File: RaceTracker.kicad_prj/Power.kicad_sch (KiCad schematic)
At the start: 41 parts, among them J1 USB-C Sink, J7 LiPo, Q2 SIA817, Q3 2N7002, U3 AP2112K-3.3 -> +3V3D, U5 BQ24195L, U6 AP2112K-3.3 -> +3V3

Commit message: Footprints für Power+MCU_Radio: aus MKR1010-Eagle-Referenz importiert
Nutzt kicad-cli pcb import, um die reale MKR-WiFi-1010-Platine
(user-bereitgestellt, MKRWiFi1010V2.0.brd) nach KiCad zu konvertieren
und daraus bewährte, aus einem tatsächlich gefertigten Board stammende
Footprint-Geometrien zu extrahieren statt sie zu schätzen:

- 15 spezielle Footprints neu in RaceTracker.pretty/ (SOT-143B für D1,
  SOD-323FL für D2/D3, SOT-523 für Q1/Q3, SON-8 für Q2, SOT-363 für Q5,
  JST-PH für J7, PTS820-Taster, 0603-LED, RGB-5050-LED, SRP4020-Spule,
  32.768kHz-Quarz ABS07)
- 3 bestehende Custom-Footprints (QFN24, QFN48/SAMD21, NINA-W1X) durch
  die vollständigeren Eagle-Varianten ersetzt (identische Pad-Namen
  verifiziert, jetzt mit Silkscreen-Outline und Lötstoppmasken-Angaben)
- Alle Standard-Passiva (R/C 0402/0603/0805, Fuse, Ferritperle) auf
  KiCads Standardbibliothek gemappt
- J12 (SWD-Header) auf Standard-2,54mm-5-Pin-Stiftleiste gemappt

87 von 90 Bauteilen auf Power+MCU_Radio haben jetzt ein Footprint
(Rest: GPS- und Sensors_Storage-Blatt folgen). ERC weiterhin 0/0,
inklusive der Footprint-Bibliotheksprüfung (jeder Footprint-Name
gegen die echte Bibliothek verifiziert).

Co-Authored-By: Claude Sonnet 5 <noreply@anthropic.com>
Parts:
- C1: footprint (none) -> Capacitor_SMD:C_0805_2012Metric
- C12, C13, C19, C20: footprint (none) -> Capacitor_SMD:C_0603_1608Metric
- C14, C15, C16, C22, C32, C33, C34, C8, C9: footprint (none) -> Capacitor_SMD:C_0402_1005Metric
- D1: footprint (none) -> RaceTracker:SOT143B_4N
- D2, D3: footprint (none) -> RaceTracker:SODFL3517X110N
- DL2, DL3: footprint (none) -> RaceTracker:LED_0603_AK
- F1, F2: footprint (none) -> Fuse:Fuse_0603_1608Metric
- J7: footprint (none) -> RaceTracker:JST_S2B_PH_SM4_TB
- L2: footprint (none) -> RaceTracker:SRP4020
- Q2: footprint (none) -> RaceTracker:SON65P205X205X75-8N-MWSD
- Q3: footprint (none) -> RaceTracker:SOTFL50P160X78-3
- R1, R19, R23, R24, R25, R26, R27, R28, R29, R30, R37, R38: footprint (none) -> Resistor_SMD:R_0402_1005Metric
- U3, U6: footprint (none) -> RaceTracker:SOT25
- U5: footprint (none) -> RaceTracker:QFN24_BQ24195L
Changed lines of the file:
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@@
 			)
 		)
-		(property "Footprint" ""
+		(property "Footprint" "Resistor_SMD:R_0402_1005Metric"
 			(at 134.62 43.18 0)
 			(hide yes)
@@
 			)
 		)
-		(property "Footprint" ""
+		(property "Footprint" "RaceTracker:SODFL3517X110N"
 			(at 248.92 43.18 0)
 			(hide yes)
@@
 			)
 		)
-		(property "Footprint" ""
+		(property "Footprint" "Capacitor_SMD:C_0402_1005Metric"
 			(at 170.18 97.79 0)
 			(hide yes)
@@
 			)
 		)
-		(property "Footprint" ""
+		(property "Footprint" "RaceTracker:SOT25"
 			(at 297.18 152.4 0)
 			(hide yes)
@@
 			)
 		)
-		(property "Footprint" ""
+		(property "Footprint" "Capacitor_SMD:C_0402_1005Metric"
 			(at 231.14 97.79 0)
 			(hide yes)
@@
 			)
 		)
-		(property "Footprint" ""
+		(property "Footprint" "RaceTracker:SRP4020"
 			(at 68.58 97.79 0)
 			(hide yes)
@@
 			)
 		)
-		(property "Footprint" ""
+		(property "Footprint" "RaceTracker:SODFL3517X110N"
 			(at 372.11 43.18 0)
 			(hide yes)
@@
 			)
 		)
-		(property "Footprint" ""
+		(property "Footprint" "RaceTracker:SOT143B_4N"
 			(at 67.31 43.18 0)
 			(hide yes)
@@
 			)
 		)
-		(property "Footprint" ""
+		(property "Footprint" "RaceTracker:SOT25"
 			(at 251.46 152.4 0)
 			(hide yes)
@@
 			)
 		)
-		(property "Footprint" ""
+		(property "Footprint" "Capacitor_SMD:C_0402_1005Metric"
 			(at 330.2 152.4 0)
 			(hide yes)
@@
 			)
 		)
-		(property "Footprint" ""
+		(property "Footprint" "RaceTracker:SON65P205X205X75-8N-MWSD"
 			(at 275.59 43.18 0)
 			(hide yes)
@@
 			)
 		)
-		(property "Footprint" ""
+		(property "Footprint" "Capacitor_SMD:C_0603_1608Metric"
 			(at 109.22 97.79 0)
 			(hide yes)
@@
 			)
 		)
-		(property "Footprint" ""
+		(property "Footprint" "Resistor_SMD:R_0402_1005Metric"
 			(at 93.98 43.18 0)
 			(hide yes)
@@
 			)
 		)
-		(property "Footprint" ""
+		(property "Footprint" "Resistor_SMD:R_0402_1005Metric"
 			(at 154.94 43.18 0)
 			(hide yes)
@@
 			)
 		)
-		(property "Footprint" ""
+		(property "Footprint" "Resistor_SMD:R_0402_1005Metric"
 			(at 83.82 152.4 0)
 			(hide yes)
@@
 			)
 		)
-		(property "Footprint" ""
+		(property "Footprint" "Capacitor_SMD:C_0603_1608Metric"
 			(at 129.54 97.79 0)
 			(hide yes)
@@
 			)
 		)
-		(property "Footprint" ""
+		(property "Footprint" "Capacitor_SMD:C_0402_1005Metric"
 			(at 251.46 97.79 0)
 			(hide yes)
@@
 			)
 		)
-		(property "Footprint" ""
+		(property "Footprint" "Capacitor_SMD:C_0603_1608Metric"
 			(at 210.82 97.79 0)
 			(hide yes)
@@
 			)
 		)
-		(property "Footprint" ""
+		(property "Footprint" "Capacitor_SMD:C_0402_1005Metric"
 			(at 350.52 152.4 0)
 			(hide yes)
@@
 			)
 		)
-		(property "Footprint" ""
+		(property "Footprint" "RaceTracker:LED_0603_AK"
 			(at 124.46 152.4 0)
 			(hide yes)
@@
 			)
 		)
-		(property "Footprint" ""
+		(property "Footprint" "Resistor_SMD:R_0402_1005Metric"
 			(at 22.86 152.4 0)
 			(hide yes)
@@
 			)
 		)
-		(property "Footprint" ""
+		(property "Footprint" "RaceTracker:SON65P205X205X75-8N-MWSD"
 			(at 304.8 43.18 0)
 			(hide yes)
@@
 			)
 		)
-		(property "Footprint" ""
+		(property "Footprint" "Fuse:Fuse_0603_1608Metric"
 			(at 175.26 43.18 0)
 			(hide yes)
@@
 			)
 		)
-		(property "Footprint" ""
+		(property "Footprint" "Capacitor_SMD:C_0603_1608Metric"
 			(at 190.5 97.79 0)
 			(hide yes)
@@
 			)
 		)
-		(property "Footprint" ""
+		(property "Footprint" "RaceTracker:LED_0603_AK"
 			(at 351.79 43.18 0)
 			(hide yes)
@@
 			)
 		)
-		(property "Footprint" ""
+		(property "Footprint" "Resistor_SMD:R_0402_1005Metric"
 			(at 63.5 152.4 0)
 			(hide yes)
@@
 			)
 		)
-		(property "Footprint" ""
+		(property "Footprint" "Resistor_SMD:R_0402_1005Metric"
 			(at 165.1 152.4 0)
 			(hide yes)
@@
 			)
 		)
-		(property "Footprint" ""
+		(property "Footprint" "Resistor_SMD:R_0402_1005Metric"
 			(at 218.44 152.4 0)
 			(hide yes)
@@
 			)
 		)
-		(property "Footprint" ""
+		(property "Footprint" "RaceTracker:JST_S2B_PH_SM4_TB"
 			(at 201.93 43.18 0)
 			(hide yes)
@@
 			)
 		)
-		(property "Footprint" ""
+		(property "Footprint" "RaceTracker:SOTFL50P160X78-3"
 			(at 191.77 152.4 0)
 			(hide yes)
@@
 			)
 		)
-		(property "Footprint" ""
+		(property "Footprint" "RaceTracker:QFN24_BQ24195L"
 			(at 35.56 97.79 0)
 			(hide yes)
@@
 			)
 		)
-		(property "Footprint" ""
+		(property "Footprint" "Capacitor_SMD:C_0402_1005Metric"
 			(at 370.84 152.4 0)
 			(hide yes)
@@
 			)
 		)
-		(property "Footprint" ""
+		(property "Footprint" "Fuse:Fuse_0603_1608Metric"
 			(at 228.6 43.18 0)
 			(hide yes)
@@
 			)
 		)
-		(property "Footprint" ""
+		(property "Footprint" "Capacitor_SMD:C_0805_2012Metric"
 			(at 114.3 43.18 0)
 			(hide yes)
@@
 			)
 		)
-		(property "Footprint" ""
+		(property "Footprint" "Capacitor_SMD:C_0402_1005Metric"
 			(at 20.32 29.21 0)
 			(hide yes)
@@
 			)
 		)
-		(property "Footprint" ""
+		(property "Footprint" "Resistor_SMD:R_0402_1005Metric"
 			(at 331.47 43.18 0)
 			(hide yes)
@@
 			)
 		)
-		(property "Footprint" ""
+		(property "Footprint" "Capacitor_SMD:C_0402_1005Metric"
 			(at 149.86 97.79 0)
 			(hide yes)
@@
 			)
 		)
-		(property "Footprint" ""
+		(property "Footprint" "Resistor_SMD:R_0402_1005Metric"
 			(at 104.14 152.4 0)
 			(hide yes)
@@
 			)
 		)
-		(property "Footprint" ""
+		(property "Footprint" "Resistor_SMD:R_0402_1005Metric"
 			(at 43.18 152.4 0)
 			(hide yes)
@@
 			)
 		)
-		(property "Footprint" ""
+		(property "Footprint" "Resistor_SMD:R_0402_1005Metric"
 			(at 144.78 152.4 0)
 			(hide yes)
@@
 			)
 		)
-		(property "Footprint" ""
+		(property "Footprint" "Capacitor_SMD:C_0402_1005Metric"
 			(at 88.9 97.79 0)
 			(hide yes)

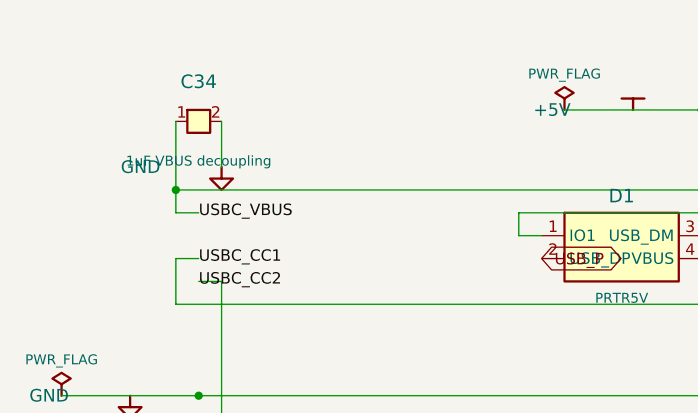
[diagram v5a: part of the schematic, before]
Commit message: D4: TVS-Diode für VBUS-ESD-Schutz an J1 ergänzt
Löst die zuvor offen gelassene Bauteilfrage (UC-002 aus der
kicad-happy-Analyse: kein ESD-Schutz auf der VBUS-Leitung, D1 deckt
nur D+/D- ab).

Nexperia PESD5V0S1BA (LCSC C5261083, SOD-323), unidirektionale 5V-TVS,
166k Stück verfügbar. Kathode an USBC_VBUS, Anode an GND — klemmt
Überspannungstransienten von VBUS nach Masse ab.

ERC weiterhin 0 Fehler/0 Warnungen, Verbindung per Netzliste verifiziert.

Co-Authored-By: Claude Sonnet 5 <noreply@anthropic.com>
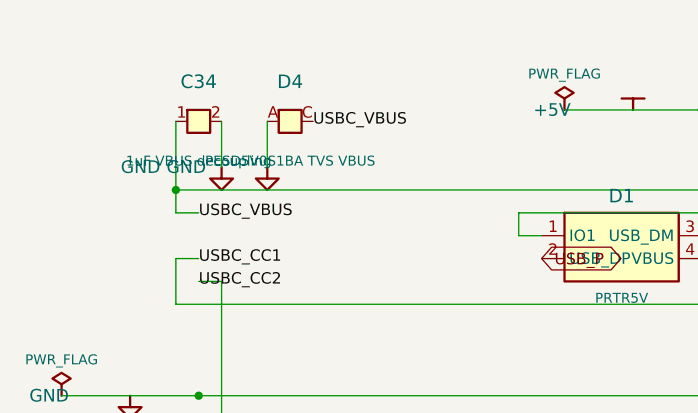
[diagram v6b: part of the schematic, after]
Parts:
- added D4: PESD5V0S1BA TVS VBUS, Diode_SMD:D_SOD-323, symbol RaceTracker:DIODE_AC
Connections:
- net GND: now also D4.A
- net USBC_VBUS: now also D4.C
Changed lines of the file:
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@@
+		)
+	)
+	(label "USBC_VBUS"
+		(at 33.02 29.21 0)
+		(effects
+			(font
+				(size 1.27 1.27)
+			)
+			(justify left)
+		)
+	)
+	(wire
+		(pts
+			(xy 27.94 29.21) (xy 27.94 34.29)
+		)
+		(stroke
+			(width 0)
+			(type default)
 		)
 	)
@@
 				(path "/91b37a92-c006-41eb-be41-a2390c5c45b2/48e8423c-d46f-487f-85bb-35381b682ff2"
 					(reference "#PWR104")
+					(unit 1)
+				)
+			)
+		)
+	)
+	(symbol
+		(lib_id "RaceTracker:GND")
+		(at 27.94 34.29 0)
+		(unit 1)
+		(body_style 1)
+		(exclude_from_sim no)
+		(in_bom no)
+		(on_board no)
+		(in_pos_files yes)
+		(dnp no)
+		(property "Reference" "#PWR105"
+			(at 27.94 41.29 0)
+			(show_name no)
+			(do_not_autoplace no)
+			(hide yes)
+			(effects
+				(font
+					(size 1.27 1.27)
+				)
+			)
+		)
+		(property "Value" "GND"
+			(at 18.94 34.29 0)
+			(show_name no)
+			(do_not_autoplace no)
+			(effects
+				(font
+					(size 1.4 1.4)
+				)
+			)
+		)
+		(property "Footprint" ""
+			(at 27.94 34.29 0)
+			(show_name no)
+			(do_not_autoplace no)
+			(effects
+				(font
+					(size 1.27 1.27)
+				)
+			)
+		)
+		(property "Datasheet" ""
+			(at 27.94 34.29 0)
+			(show_name no)
+			(do_not_autoplace no)
+			(effects
+				(font
+					(size 1.27 1.27)
+				)
+			)
+		)
+		(property "Description" ""
+			(at 27.94 34.29 0)
+			(show_name no)
+			(do_not_autoplace no)
+			(effects
+				(font
+					(size 1.27 1.27)
+				)
+			)
+		)
+		(pin "1"
+		)
+		(instances
+			(project "RaceTracker"
+				(path "/91b37a92-c006-41eb-be41-a2390c5c45b2/48e8423c-d46f-487f-85bb-35381b682ff2"
+					(reference "#PWR105")
 					(unit 1)
 				)
@@
 					(unit 1)
 				)
+			)
+		)
+	)
+	(symbol
+		(lib_id "RaceTracker:DIODE_AC")
+		(at 30.48 29.21 0)
+		(unit 1)
+		(body_style 1)
+		(exclude_from_sim no)
+		(in_bom yes)
+		(on_board yes)
+		(in_pos_files yes)
+		(dnp no)
+		(property "Reference" "D4"
+			(at 30.48 24.81 0)
+			(show_name no)
+			(do_not_autoplace no)
+			(effects
+				(font
+					(size 1.5 1.5)
+				)
+			)
+		)
+		(property "Value" "PESD5V0S1BA TVS VBUS"
+			(at 30.48 33.61 0)
+			(show_name no)
+			(do_not_autoplace no)
+			(effects
+				(font
+					(size 1.1 1.1)
+				)
+			)
+		)
+		(property "Footprint" "Diode_SMD:D_SOD-323"
+			(at 30.48 29.21 0)
+			(hide yes)
+			(show_name no)
+			(do_not_autoplace no)
+			(effects
+				(font
+					(size 1.27 1.27)
+				)
+			)
+		)
+		(property "Datasheet" ""
+			(at 30.48 29.21 0)
+			(hide yes)
+			(show_name no)
+			(do_not_autoplace no)
+			(effects
+				(font
+					(size 1.27 1.27)
+				)
+			)
+		)
+		(property "Description" ""
+			(at 30.48 29.21 0)
+			(show_name no)
+			(do_not_autoplace no)
+			(effects
+				(font
+					(size 1.27 1.27)
+				)
+			)
+		)
+		(property "MPN" "PESD5V0S1BA"
+			(at 30.48 29.21 0)
+			(hide yes)
+			(show_name no)
+			(do_not_autoplace no)
+			(effects
+				(font
+					(size 1.27 1.27)
+				)
+			)
+		)
+		(property "Manufacturer" "Nexperia"
+			(at 30.48 29.21 0)
+			(hide yes)
+			(show_name no)
+			(do_not_autoplace no)
+			(effects
+				(font
+					(size 1.27 1.27)
+				)
+			)
+		)
+		(pin "A"
+		)
+		(pin "C"
+		)
+		(instances
+			(project "RaceTracker"
+				(path "/91b37a92-c006-41eb-be41-a2390c5c45b2/48e8423c-d46f-487f-85bb-35381b682ff2"
+					(reference "D4")
+					(unit 1)
+				)
